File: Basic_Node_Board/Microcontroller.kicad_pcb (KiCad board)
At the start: 4 copper layers, 100 x 100 mm, 31 parts, among them J1 Conn_01x02, J4 Conn_01x02_Pin, U2 ESP32-DEVKIT-C, U3 TPS54560BQDDARQ1, U6 TJA1050T/CM,118

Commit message: breif mockup of the mcu board
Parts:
- added J2: Conn_01x19_Socket, Connector_Pin:Pin_D1.0mm_L10.0mm, F.Cu at (6.67, 1.52)
- added J3: Conn_01x19_Socket, Connector_Pin:Pin_D1.0mm_L10.0mm, F.Cu at (6.67, 5.58)
- added U4: AP64060WU-7, Package_TO_SOT_SMD:TSOT-23-6, F.Cu at (2.08, 1.90)
- added U5: AP64060WU-7, Package_TO_SOT_SMD:TSOT-23-6, F.Cu at (2.08, 6.53)
- L1: footprint Inductor_SMD:L_1206_3216Metric_Pad1.22x1.90mm_HandSolder -> Inductor_SMD:L_Coilcraft_LPS3010
- moved L1 1.80 mm to (75.0, 27.5)

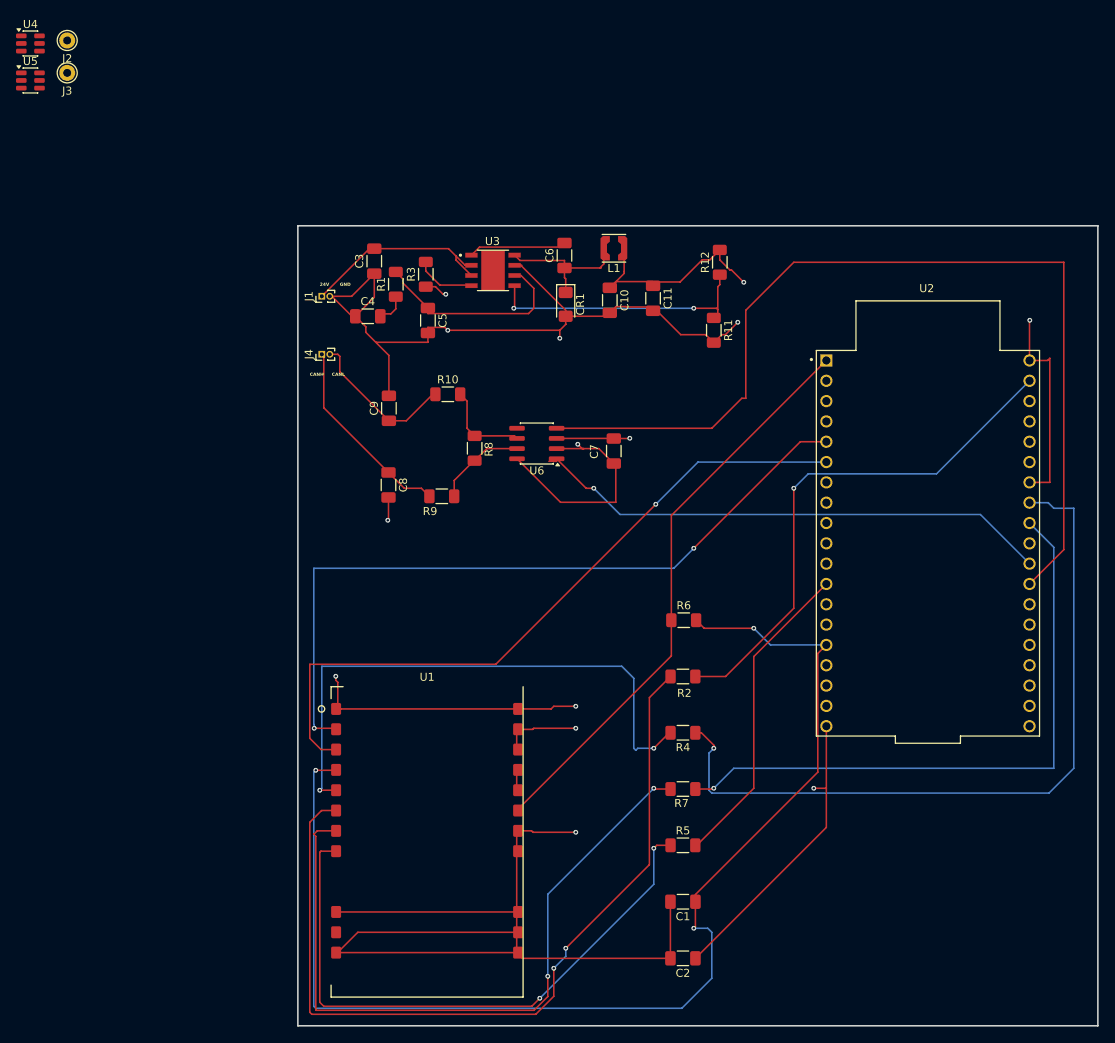
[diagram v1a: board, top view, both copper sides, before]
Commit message: made changes to some footprints and overall layout of the board (in line with TI buck recomendations)
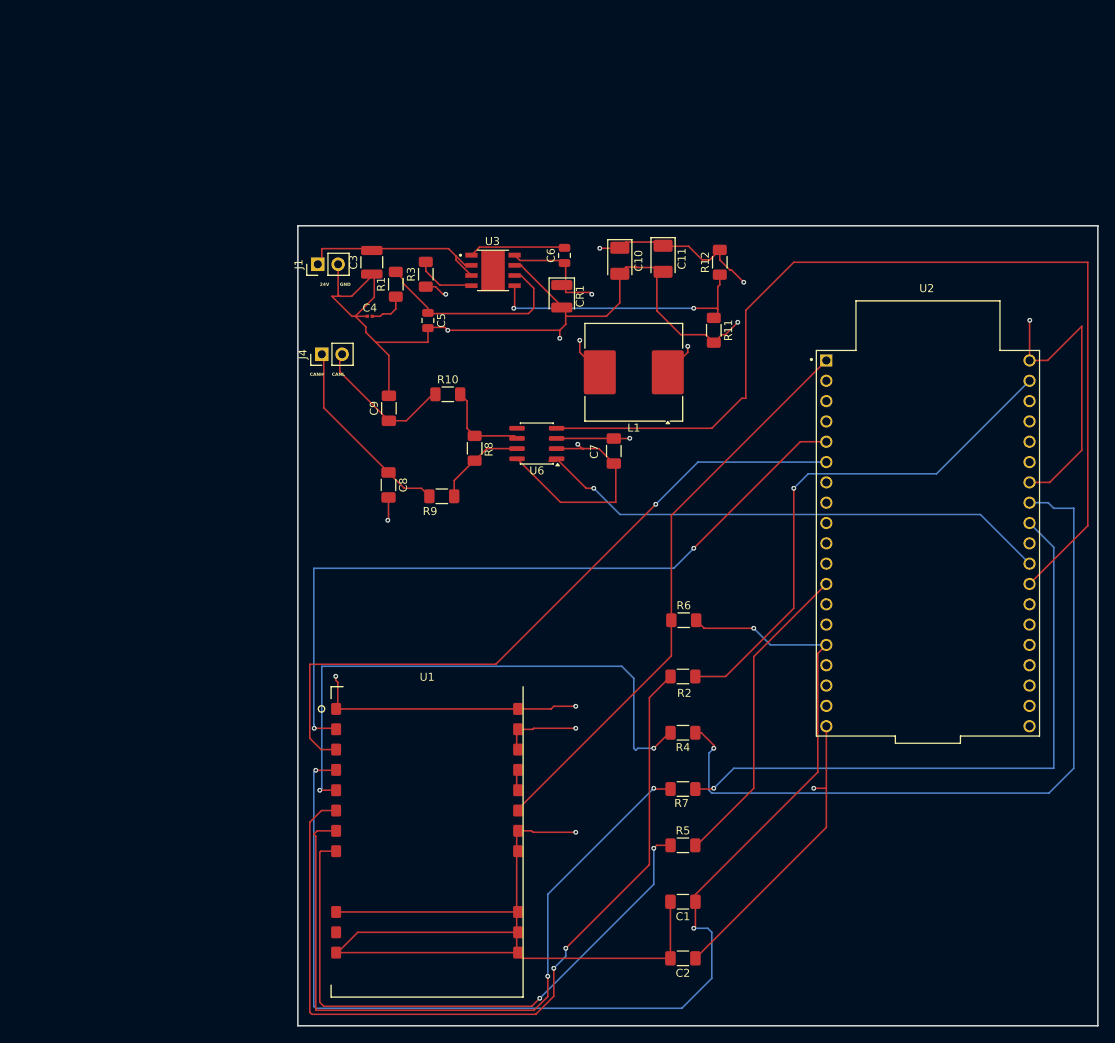
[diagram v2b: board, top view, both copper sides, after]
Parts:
- removed J2, J3: Conn_01x19_Socket, Connector_Pin:Pin_D1.0mm_L10.0mm
- removed U4, U5: AP64060WU-7, Package_TO_SOT_SMD:TSOT-23-6
- C10, C11: footprint Capacitor_SMD:C_1206_3216Metric_Pad1.33x1.80mm_HandSolder -> Capacitor_Tantalum_SMD:CP_EIA-3528-21_Kemet-B_HandSolder
- C3: footprint Capacitor_SMD:C_1206_3216Metric_Pad1.33x1.80mm_HandSolder -> Capacitor_SMD:C_1210_3225Metric
- C4: footprint Capacitor_SMD:C_1206_3216Metric_Pad1.33x1.80mm_HandSolder -> Capacitor_SMD:C_0201_0603Metric
- C5, C6: footprint Capacitor_SMD:C_1206_3216Metric_Pad1.33x1.80mm_HandSolder -> Capacitor_SMD:C_0805_2012Metric
- CR1: footprint Diode_SMD:D_1206_3216Metric_Pad1.42x1.75mm_HandSolder -> Diode_SMD:D_1210_3225Metric
- J1, J4: footprint Connector_PinHeader_1.00mm:PinHeader_1x02_P1.00mm_Vertical -> Connector_PinHeader_2.54mm:PinHeader_1x02_P2.54mm_Vertical
- L1: footprint Inductor_SMD:L_Coilcraft_LPS3010 -> Inductor_SMD:L_Coilcraft_MSS1260T-XXX
- moved L1 15.7 mm to (77.5, 43.0)
- moved C10 5.09 mm to (75.8, 29.1)
- moved C11 5.09 mm to (81.2, 28.8)
- moved J1 4.03 mm to (38.0, 29.5)
- moved CR1 1.12 mm to (68.5, 33.5)
- moved C3 0.34 mm to (44.8, 29.2)
- moved C4 0.25 mm to (44.5, 36.0)
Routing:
- net GND: track 468.5 -> 495.7 mm
- net 5.3V OUT: track 190.1 -> 206.2 mm, vias 4 -> 6
- net Net-(U3-SW): track 17.8 -> 24.7 mm, vias 0 -> 2
- net Net-(J3-Pin_12): track 120.4 -> 124.7 mm
- net /CANL: track 19.1 -> 18.1 mm
- net Net-(C4-Pad2): track 3.85 -> 4.84 mm
- net /24V: track 25.6 -> 24.9 mm
- removed copper zone on In2.Cu, net GND

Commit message: fixed the buck converter
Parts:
- moved C2 50.7 mm to (52.2, 76.5)
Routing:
- net 5.3V OUT: track 206.2 -> 203.6 mm, vias 6 -> 7
- net GND: track 495.7 -> 497.3 mm, vias 10 -> 11
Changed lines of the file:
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@@
 	(footprint "Capacitor_SMD:C_1206_3216Metric_Pad1.33x1.80mm_HandSolder"
 		(layer "F.Cu")
-		(at 83.6416 116.257333 180)
+		(at 52.25 76.5 180)
 		(descr "Capacitor SMD 1206 (3216 Metric), square (rectangular) end terminal, IPC-7351 nominal with elongated pad for handsoldering. (Body size source: IPC-SM-782 page 76, https://www.pcb-3d.com/wordpress/wp-content/uploads/ipc-sm-782a_amendment_1_and_2.pdf), generated with kicad-footprint-generator")
 		(tags "capacitor handsolder")
@@
 	)
 	(segment
+		(start 69.75 117.5)
+		(end 78.066934 109.183066)
+		(width 0.2)
+		(layer "F.Cu")
+		(net 1)
+	)
+	(segment
 		(start 133.5 37.25)
 		(end 129.228 41.522)
@@
 	)
 	(segment
-		(start 82.0791 116.257333)
-		(end 63.579333 116.257333)
-		(width 0.2)
-		(layer "F.Cu")
-		(net 1)
-	)
-	(segment
 		(start 68.9864 35.9941)
 		(end 74.0684 35.9941)
@@
 	)
 	(segment
+		(start 50.6875 76.5)
+		(end 48.5 76.5)
+		(width 0.2)
+		(layer "F.Cu")
+		(net 1)
+	)
+	(segment
 		(start 45.25 39.25)
 		(end 46.8872 40.8872)
@@
 	)
 	(segment
-		(start 82.0791 109.183066)
-		(end 82.0791 116.257333)
-		(width 0.2)
-		(layer "F.Cu")
-		(net 1)
-	)
-	(segment
 		(start 68.9864 35.2392)
 		(end 68.9864 35.9941)
@@
 	)
 	(segment
+		(start 63.0386 115.5416)
+		(end 67.7916 115.5416)
+		(width 0.2)
+		(layer "F.Cu")
+		(net 1)
+	)
+	(segment
 		(start 40.496 85.0816)
 		(end 40.6908 84.8868)
@@
 	)
 	(segment
+		(start 78.066934 109.183066)
+		(end 82.0791 109.183066)
+		(width 0.2)
+		(layer "F.Cu")
+		(net 1)
+	)
+	(segment
 		(start 40.25 81)
 		(end 40.25 81.5)
@@
 	)
 	(segment
+		(start 67.7916 115.5416)
+		(end 69.75 117.5)
+		(width 0.2)
+		(layer "F.Cu")
+		(net 1)
+	)
+	(segment
 		(start 40.5 85.0452)
 		(end 40.4636 85.0816)
@@
 	)
 	(via
+		(at 48.5 76.5)
+		(size 0.6)
+		(drill 0.3)
+		(layers "F.Cu" "B.Cu")
+		(net 1)
+	)
+	(via
 		(at 127 36.5)
 		(size 0.6)
@@
 	)
 	(segment
+		(start 48.5 76.5)
+		(end 46.75 76.5)
+		(width 0.2)
+		(layer "In2.Cu")
+		(net 1)
+	)
+	(segment
 		(start 68.25 98.5)
 		(end 70.25 100.5)
@@
 	)
 	(segment
+		(start 46.75 77.25)
+		(end 46.75 76.5)
+		(width 0.2)
+		(layer "In2.Cu")
+		(net 1)
+	)
+	(segment
 		(start 69.75 85.25)
 		(end 68.5 85.25)
@@
 	)
 	(segment
-		(start 46.75 77.25)
+		(start 46.75 76.5)
 		(end 46.75 61.5)
 		(width 0.2)
@@
 	)
 	(segment
-		(start 101.5677 99.893733)
-		(end 101.5677 95)
-		(width 0.2)
-		(layer "F.Cu")
-		(net 53)
-	)
-	(segment
 		(start 88.25 28.95)
 		(end 88.25 27.7)
@@
 	)
 	(segment
+		(start 53.8125 76.5)
+		(end 56 76.5)
+		(width 0.2)
+		(layer "F.Cu")
+		(net 53)
+	)
+	(segment
 		(start 84.25 40.5)
 		(end 84.25 39.75)
@@
 	)
 	(segment
-		(start 85.2041 116.257333)
-		(end 101.5677 99.893733)
-		(width 0.2)
-		(layer "F.Cu")
-		(net 53)
-	)
-	(segment
 		(start 64.8636 87.6364)
 		(end 62.8784 87.6364)
@@
 	)
 	(via
+		(at 56 76.5)
+		(size 0.6)
+		(drill 0.3)
+		(layers "F.Cu" "B.Cu")
+		(net 53)
+	)
+	(via
 		(at 100 95)
 		(size 0.6)
@@
 	)
 	(segment
+		(start 72.5 80)
+		(end 72.5 85)
+		(width 0.2)
+		(layer "In1.Cu")
+		(net 53)
+	)
+	(segment
 		(start 77 51.25)
 		(end 96.5 70.75)
@@
 	)
 	(segment
+		(start 72.5 85)
+		(end 72.75 85.25)
+		(width 0.2)
+		(layer "In1.Cu")
+		(net 53)
+	)
+	(segment
 		(start 90.25 85.25)
 		(end 92.5 87.5)
@@
 	(segment
 		(start 72.5 85.25)
-		(end 90.25 85.25)
+		(end 72.75 85.25)
+		(width 0.2)
+		(layer "In1.Cu")
+		(net 53)
+	)
+	(segment
+		(start 69 76.5)
+		(end 72.5 80)
 		(width 0.2)
 		(layer "In1.Cu")
@@
 		(width 0.2)
 		(layer "In1.Cu")
+		(net 53)
+	)
+	(segment
+		(start 72.75 85.25)
+		(end 90.25 85.25)
+		(width 0.2)
+		(layer "In1.Cu")
+		(net 53)
+	)
+	(segment
+		(start 56 76.5)
+		(end 69 76.5)
+		(width 0.2)
+		(layer "In1.Cu")
